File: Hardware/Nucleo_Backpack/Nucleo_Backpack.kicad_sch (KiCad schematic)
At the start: 5 parts, among them J1 CN7, J2 CN10

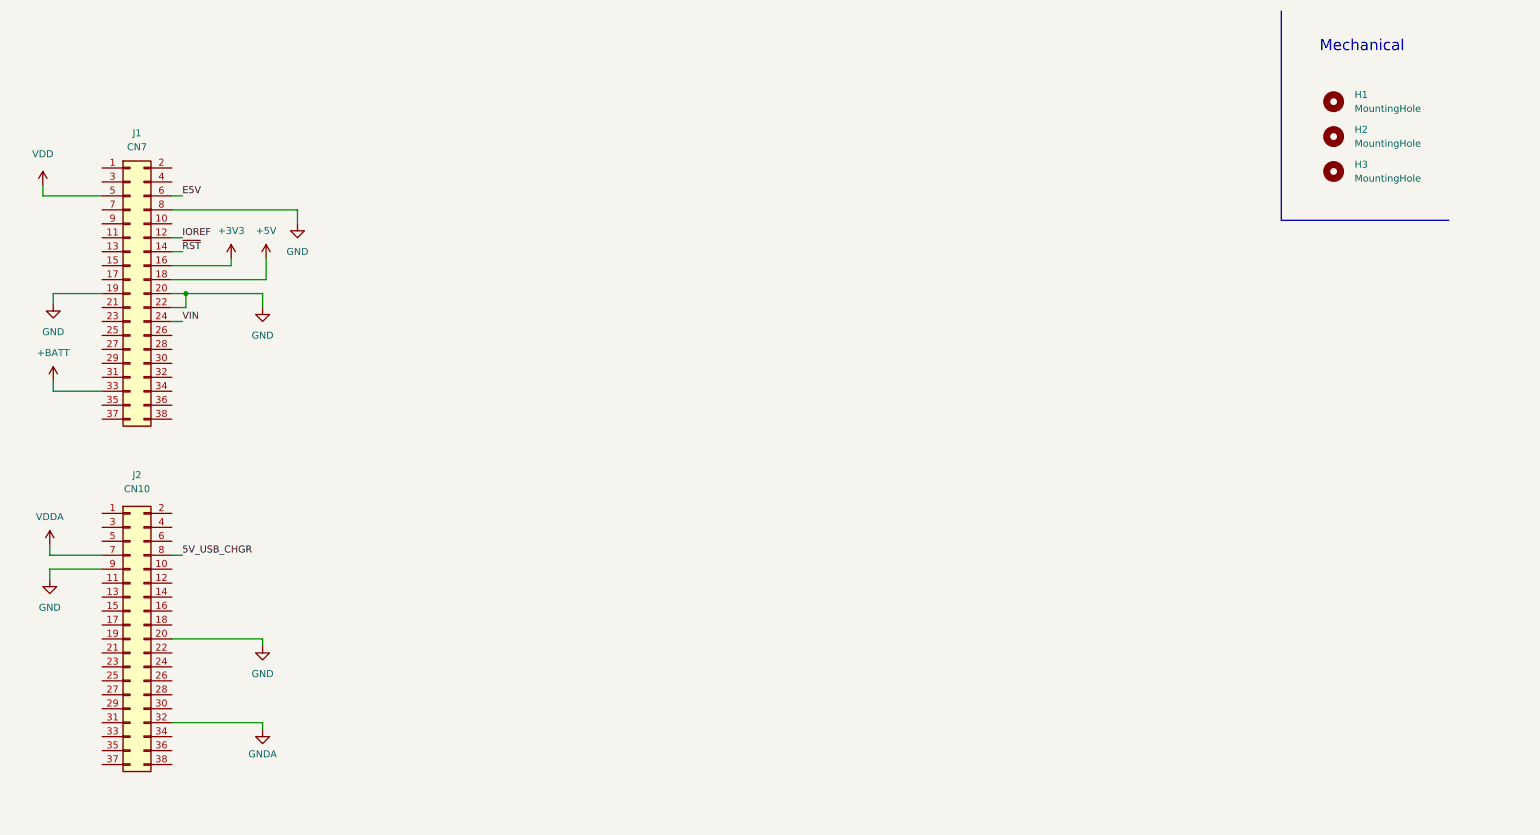
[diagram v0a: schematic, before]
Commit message: Made Beginning breakout for Nucleo Backpack
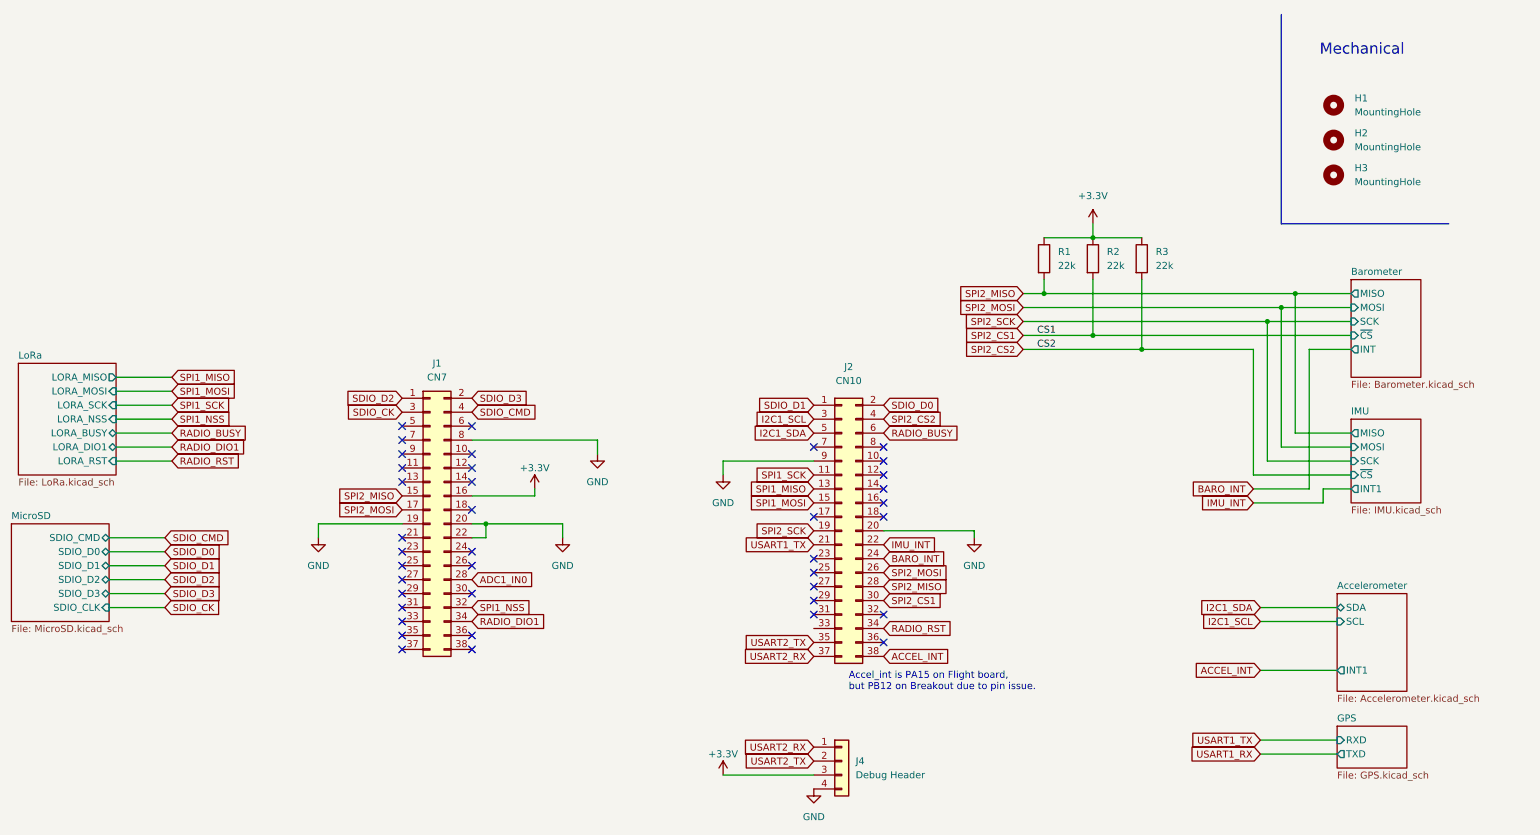
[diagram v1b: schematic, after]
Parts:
- added J4: Debug Header, symbol Connector_Generic:Conn_01x04
- added R1, R2, R3: 22k, Resistor_SMD:R_0603_1608Metric_Pad0.98x0.95mm_HandSolder, symbol Device:R
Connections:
- net GND: now also J4.4 (Pin_4)
- net SDIO_D2: now reaches J1.1 (Pin_1)
- net SPI2_MISO: now reaches J1.15 (Pin_15)
- net SPI2_MISO: now also J2.28 (Pin_28), R1.2
- net SPI2_MOSI: now reaches J1.17 (Pin_17)
- net SPI2_MOSI: now also J2.26 (Pin_26)
- net SDIO_D3: now reaches J1.2 (Pin_2)
- net ADC1_IN0: now reaches J1.28 (Pin_28)
- net SDIO_CK: now reaches J1.3 (Pin_3)
- net SPI1_NSS: now reaches J1.32 (Pin_32)
- net RADIO_DIO1: now reaches J1.34 (Pin_34)
- net SDIO_CMD: now reaches J1.4 (Pin_4)
- net SDIO_D1: now reaches J2.1 (Pin_1)
- net SPI1_SCK: now reaches J2.11 (Pin_11)
- net SPI1_MISO: now reaches J2.13 (Pin_13)
- net SPI1_MOSI: now reaches J2.15 (Pin_15)
- net SPI2_SCK: now reaches J2.19 (Pin_19)
- net SDIO_D0: now reaches J2.2 (Pin_2)
- net USART1_TX: now reaches J2.21 (Pin_21)
- net IMU_INT: now reaches J2.22 (Pin_22)
- net BARO_INT: now reaches J2.24 (Pin_24)
- net I2C1_SCL: now reaches J2.3 (Pin_3)
- net SPI2_CS1: now reaches J2.30 (Pin_30)
- net SPI2_CS1: now also R2.2
- net RADIO_RST: now reaches J2.34 (Pin_34)
- net USART2_TX: now reaches J2.35 (Pin_35)
- net USART2_TX: now also J4.2 (Pin_2)
- net USART2_RX: now reaches J2.37 (Pin_37)
- net USART2_RX: now also J4.1 (Pin_1)
- net ACCEL_INT: now reaches J2.38 (Pin_38)
- net SPI2_CS2: now reaches J2.4 (Pin_4)
- net SPI2_CS2: now also R3.2
- net I2C1_SDA: now reaches J2.5 (Pin_5)
- net RADIO_BUSY: now reaches J2.6 (Pin_6)
- net +3V3 renamed +3.3V
- net +3.3V: now also J4.3 (Pin_3), R1.1, R2.1, R3.1
- net +5V: no longer names the net of J1.18 (Pin_18)
- net +BATT: no longer names the net of J1.33 (Pin_33)
- net 5V_USB_CHGR: no longer names the net of J2.8 (Pin_8)
- net E5V: no longer names the net of J1.6 (Pin_6)
- net GNDA: no longer names the net of J2.32 (Pin_32)
- net IOREF: no longer names the net of J1.12 (Pin_12)
- net VDD: no longer names the net of J1.5 (Pin_5)
- net VDDA: no longer names the net of J2.7 (Pin_7)
- net VIN: no longer names the net of J1.24 (Pin_24)
- net ~{RST}: no longer names the net of J1.14 (Pin_14)
- no-connect marks 0 -> 39
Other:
- added sheet Accelerometer (Accelerometer.kicad_sch)
- added sheet Barometer (Barometer.kicad_sch)
- added sheet GPS (GPS.kicad_sch)
- added sheet IMU (IMU.kicad_sch)
- added sheet LoRa (LoRa.kicad_sch)
- added sheet MicroSD (MicroSD.kicad_sch)
- note added: "Accel_int is PA15 on Flight board, but PB12 on Breakout due to pin issue."

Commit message: all components now on the backpack
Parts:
- J4: value Debug Header -> Conn_01x04; footprint (none) -> TerminalBlock_Phoenix:TerminalBlock_Phoenix_PT-1,5-4-3.5-H_1x04_P3.50mm_Horizontal
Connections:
- net USART1_RX: now also J2.33 (Pin_33)
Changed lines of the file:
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@@
+    )
+  )
+  (global_label "USART1_RX" (shape input) (at 168.91 124.46 180) (fields_autoplaced)
+    (effects (font (size 1.27 1.27)) (justify right))
+    (property "Intersheetrefs" "${INTERSHEET_REFS}" (at 155.3069 124.46 0)
+      (effects (font (size 1.27 1.27)) (justify right) hide)
     )
   )
@@
       (effects (font (size 1.27 1.27)) (justify left))
     )
-    (property "Value" "Debug Header" (at 176.53 151.13 0)
+    (property "Value" "Conn_01x04" (at 176.53 151.13 0)
       (effects (font (size 1.27 1.27)) (justify left))
     )
-    (property "Footprint" "" (at 173.99 148.59 0)
+    (property "Footprint" "TerminalBlock_Phoenix:TerminalBlock_Phoenix_PT-1,5-4-3.5-H_1x04_P3.50mm_Horizontal" (at 173.99 148.59 0)
       (effects (font (size 1.27 1.27)) hide)
     )

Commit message: Backpack Updates
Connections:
- net USART1_RX: no longer names the net of J2.33 (Pin_33)
- net USART1_TX: no longer names the net of J2.21 (Pin_21)
- no-connect marks 39 -> 41
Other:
- removed sheet GPS
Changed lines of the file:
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@@
   (no_connect (at 106.68 110.49))
   (no_connect (at 181.61 91.44))
+  (no_connect (at 168.91 109.22))
   (no_connect (at 106.68 118.11))
   (no_connect (at 106.68 92.71))
@@
   (no_connect (at 181.61 99.06))
   (no_connect (at 181.61 127))
+  (no_connect (at 168.91 124.46))
   (wire (pts (xy 250.19 132.08) (xy 264.16 132.08))
     (stroke (width 0) (type default))
   )
-  (wire (pts (xy 250.19 144.78) (xy 264.16 144.78))
-    (stroke (width 0) (type default))
-  )
   (wire (pts (xy 248.92 73.66) (xy 248.92 96.52))
     (stroke (width 0) (type default))
@@
   )
   (wire (pts (xy 210.82 60.96) (xy 210.82 63.5))
-    (stroke (width 0) (type default))
-  )
-  (wire (pts (xy 250.19 147.32) (xy 264.16 147.32))
     (stroke (width 0) (type default))
   )
@@
     )
   )
-  (global_label "USART1_RX" (shape input) (at 250.19 147.32 180) (fields_autoplaced)
-    (effects (font (size 1.27 1.27)) (justify right))
-    (property "Intersheetrefs" "${INTERSHEET_REFS}" (at 236.5869 147.32 0)
-      (effects (font (size 1.27 1.27)) (justify right) hide)
-    )
-  )
   (global_label "BARO_INT" (shape input) (at 181.61 111.76 0) (fields_autoplaced)
     (effects (font (size 1.27 1.27)) (justify left))
@@
     )
   )
-  (global_label "USART1_TX" (shape input) (at 168.91 109.22 180) (fields_autoplaced)
-    (effects (font (size 1.27 1.27)) (justify right))
-    (property "Intersheetrefs" "${INTERSHEET_REFS}" (at 155.6093 109.22 0)
-      (effects (font (size 1.27 1.27)) (justify right) hide)
-    )
-  )
   (global_label "SPI2_SCK" (shape input) (at 168.91 106.68 180) (fields_autoplaced)
     (effects (font (size 1.27 1.27)) (justify right))
@@
     )
   )
-  (global_label "USART1_TX" (shape input) (at 250.19 144.78 180) (fields_autoplaced)
-    (effects (font (size 1.27 1.27)) (justify right))
-    (property "Intersheetrefs" "${INTERSHEET_REFS}" (at 236.8893 144.78 0)
-      (effects (font (size 1.27 1.27)) (justify right) hide)
-    )
-  )
   (global_label "SDIO_D0" (shape input) (at 181.61 83.82 0) (fields_autoplaced)
     (effects (font (size 1.27 1.27)) (justify left))
@@
     (effects (font (size 1.27 1.27)) (justify right))
     (property "Intersheetrefs" "${INTERSHEET_REFS}" (at 157.0607 86.36 0)
-      (effects (font (size 1.27 1.27)) (justify right) hide)
-    )
-  )
-  (global_label "USART1_RX" (shape input) (at 168.91 124.46 180) (fields_autoplaced)
-    (effects (font (size 1.27 1.27)) (justify right))
-    (property "Intersheetrefs" "${INTERSHEET_REFS}" (at 155.3069 124.46 0)
       (effects (font (size 1.27 1.27)) (justify right) hide)
     )
@@
       )
     )
-  )
-  (sheet (at 264.16 142.24) (size 12.7 7.62) (fields_autoplaced)
-    (stroke (width 0.1524) (type solid))
-    (fill (color 0 0 0 0.0000))
-    (property "Sheetname" "GPS" (at 264.16 141.5284 0)
-      (effects (font (size 1.27 1.27)) (justify left bottom))
-    )
-    (property "Sheetfile" "GPS.kicad_sch" (at 264.16 150.4446 0)
-      (effects (font (size 1.27 1.27)) (justify left top))
-    )
-    (pin "RXD" input (at 264.16 144.78 180)
-      (effects (font (size 1.27 1.27)) (justify left))
-    )
-    (pin "TXD" output (at 264.16 147.32 180)
-      (effects (font (size 1.27 1.27)) (justify left))
-    )
-    (instances
-      (project "Nucleo_Backpack"
-        (path "/e8eb85d5-f1ff-4500-895d-25b9ff5f6d36" (page "5"))
-      )
-    )
